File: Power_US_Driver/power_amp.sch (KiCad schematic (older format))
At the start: 9 parts, among them J2 Conn_Coaxial, Q1 Q_NMOS_DGS, Q2 Q_NMOS_DGS, U2 IR2110

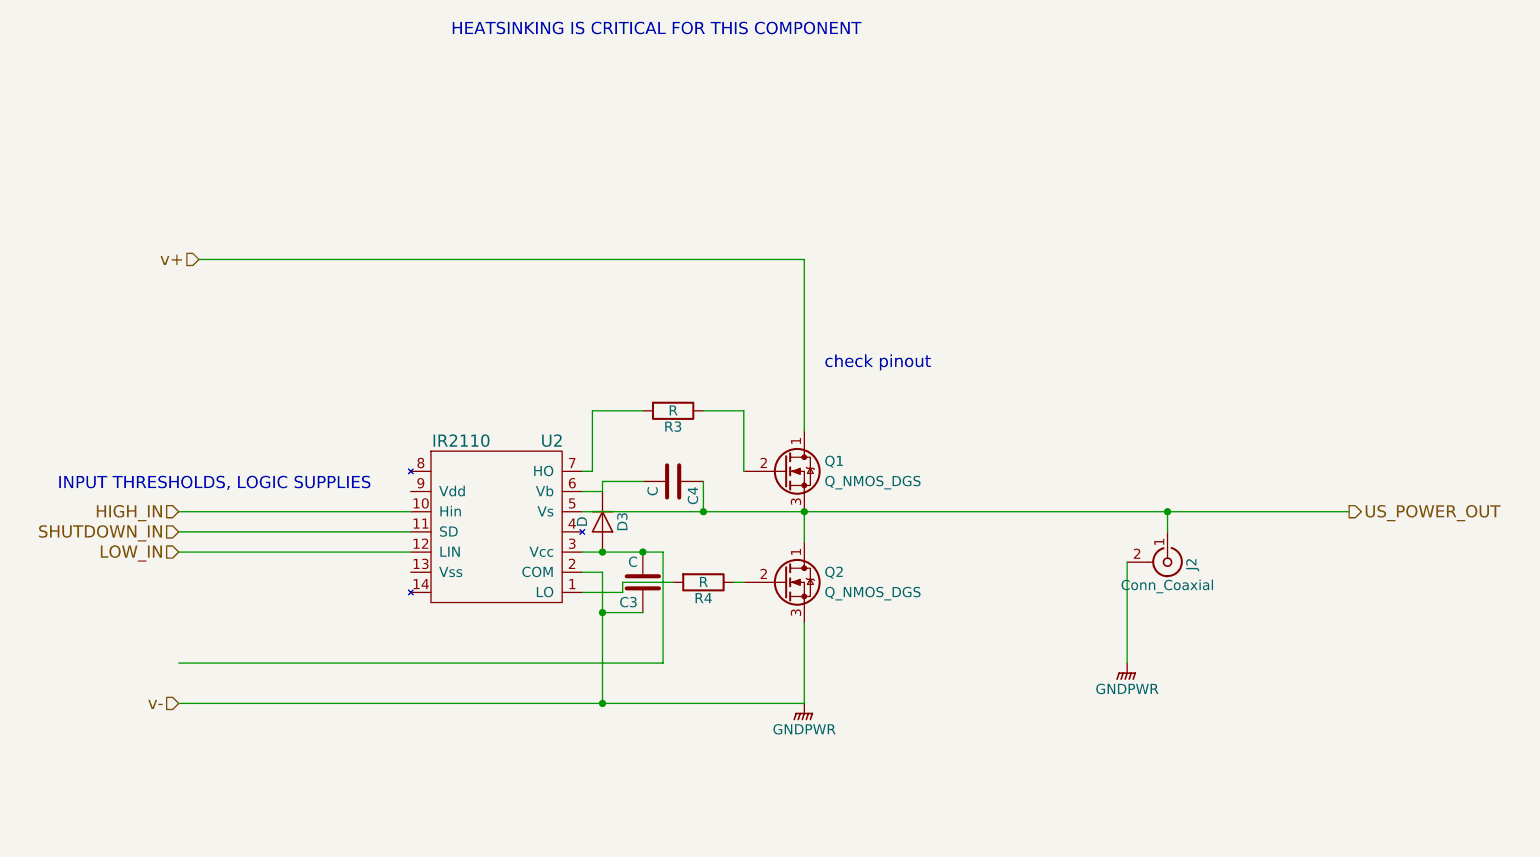
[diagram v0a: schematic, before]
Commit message: CURRENT SENSE REROUT, HIGHSIDE DRIVER GROUNDING
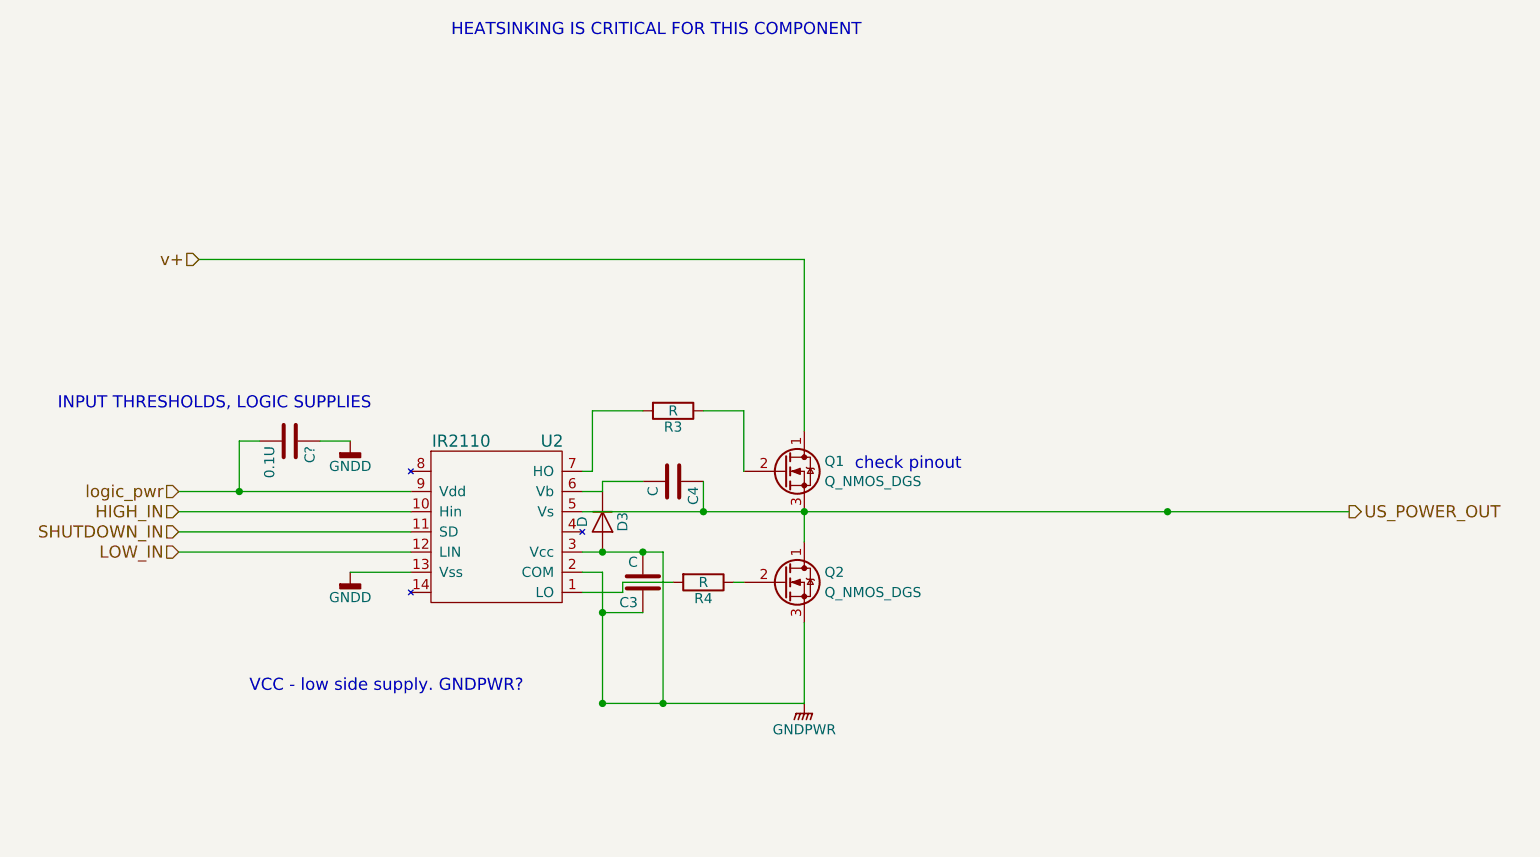
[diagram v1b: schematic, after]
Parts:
- removed J2: Conn_Coaxial, symbol Conn_Coaxial
- added C?: 0.1U, symbol C
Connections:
- net labels added: GNDD, logic_pwr
- net labels removed: v-
- wire segments 30 -> 32
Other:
- note added: "VCC - low side supply. GNDPWR?"
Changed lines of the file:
@@
 LIBS:LIA-cache
 LIBS:power_US
+LIBS:JasMoH_Parts
 LIBS:Power_US_Driver-cache
 EELAYER 25 0
@@
 Text HLabel 3250 2550 0    60   Input ~ 0
 v+
-Text HLabel 3150 4750 0    60   Input ~ 0
-v-
-$Comp
-L Conn_Coaxial J2
-U 1 1 5AADA1B5
-P 8050 4050
-F 0 "J2" H 8060 4170 50  0000 C CNN
-F 1 "Conn_Coaxial" V 8165 4050 50  0000 C CNN
-F 2 "" H 8050 4050 50  0001 C CNN
-F 3 "" H 8050 4050 50  0001 C CNN
-	1    8050 4050
-	0    1    1    0
-$EndComp
 Text Notes 4500 1450 0    60   ~ 0
 HEATSINKING IS CRITICAL FOR THIS COMPONENT
@@
 	1    0    0    -1
 $EndComp
-Text Notes 6350 3100 0    60   ~ 0
+Text Notes 6500 3600 0    60   ~ 0
 check pinout
 $Comp
@@
 $EndComp
 Wire Wire Line
-	7850 4550 7850 4050
-Wire Wire Line
-	8050 3800 8050 3900
-Wire Wire Line
 	5150 3800 8950 3800
 Wire Wire Line
@@
 Wire Wire Line
 	6250 4750 6250 4350
-Wire Wire Line
-	3150 4750 6250 4750
 Connection ~ 8050 3800
 Wire Wire Line
@@
 Connection ~ 5250 4000
 Wire Wire Line
-	5550 4000 5550 4550
-Wire Wire Line
-	5550 4550 3150 4550
+	5550 4000 5550 4750
 Connection ~ 5450 4000
-Text Notes 2550 3700 0    60   ~ 0
+Text Notes 2550 3300 0    60   ~ 0
 INPUT THRESHOLDS, LOGIC SUPPLIES
 $Comp
-L GNDPWR #PWR?
+L GNDPWR #PWR8
 U 1 1 5AB00C48
 P 6250 4750
-F 0 "#PWR?" H 6250 4550 50  0001 C CNN
+F 0 "#PWR8" H 6250 4550 50  0001 C CNN
 F 1 "GNDPWR" H 6250 4620 50  0000 C CNN
 F 2 "" H 6250 4700 50  0001 C CNN
@@
 $EndComp
 $Comp
-L GNDPWR #PWR?
-U 1 1 5AB01180
-P 7850 4550
-F 0 "#PWR?" H 7850 4350 50  0001 C CNN
-F 1 "GNDPWR" H 7850 4420 50  0000 C CNN
-F 2 "" H 7850 4500 50  0001 C CNN
-F 3 "" H 7850 4500 50  0001 C CNN
-	1    7850 4550
-	1    0    0    -1
-$EndComp
+L GNDD #PWR?
+U 1 1 5AB1B5F8
+P 4000 4100
+F 0 "#PWR?" H 4000 3850 50  0001 C CNN
+F 1 "GNDD" H 4000 3975 50  0000 C CNN
+F 2 "" H 4000 4100 50  0001 C CNN
+F 3 "" H 4000 4100 50  0001 C CNN
+	1    4000 4100
+	1    0    0    -1
+$EndComp
+Wire Wire Line
+	4300 4100 4000 4100
+Text HLabel 3150 3700 0    60   Input ~ 0
+logic_pwr
+Wire Wire Line
+	3150 3700 4300 3700
+Text Notes 3500 4700 0    60   ~ 0
+VCC - low side supply. GNDPWR?
+$Comp
+L C C?
+U 1 1 5AB1B9D2
+P 3700 3450
+F 0 "C?" H 3725 3550 50  0000 L CNN
+F 1 "0.1U" H 3725 3350 50  0000 L CNN
+F 2 "" H 3738 3300 50  0001 C CNN
+F 3 "" H 3700 3450 50  0001 C CNN
+	1    3700 3450
+	0    1    1    0
+$EndComp
+$Comp
+L GNDD #PWR?
+U 1 1 5AB1BA1D
+P 4000 3450
+F 0 "#PWR?" H 4000 3200 50  0001 C CNN
+F 1 "GNDD" H 4000 3325 50  0000 C CNN
+F 2 "" H 4000 3450 50  0001 C CNN
+F 3 "" H 4000 3450 50  0001 C CNN
+	1    4000 3450
+	1    0    0    -1
+$EndComp
+Wire Wire Line
+	4000 3450 3850 3450
+Wire Wire Line
+	3550 3450 3450 3450
+Wire Wire Line
+	3450 3450 3450 3700
+Connection ~ 3450 3700
+Connection ~ 5550 4750
+Wire Wire Line
+	5250 4750 6250 4750
 $EndSCHEMATC

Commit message: initial Current sense more vacilating over power drive solution
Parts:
- gave numbers to parts that had none: 1
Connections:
- net GNDPWR: no longer C3.1, C3.2, D3.2 (A), Q2.3 (S), U2.2 (COM), U2.3 (Vcc)
- net at Q2.2 (G): no longer R4.1
- new net V-: C3.1, C3.2, D3.2 (A), Q2.3 (S), U2.2 (COM), U2.3 (Vcc)
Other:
- note added: "C, R values"
- note added: "check that -60 is ok"
- note added: "has to be dragged to V- to turn off..."
- note added: "two of these and an optoisolator?"
- moved on the sheet: R4
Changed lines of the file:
@@
 check pinout
-$Comp
-L Q_NMOS_DGS Q2
-U 1 1 5AAE8077
-P 6150 4150
-F 0 "Q2" H 6350 4200 50  0000 L CNN
-F 1 "Q_NMOS_DGS" H 6350 4100 50  0000 L CNN
-F 2 "" H 6350 4250 50  0001 C CNN
-F 3 "" H 6150 4150 50  0001 C CNN
-	1    6150 4150
-	1    0    0    -1
-$EndComp
 $Comp
 L IR2110 U2
@@
 L R R4
 U 1 1 5AAE9F5C
-P 5750 4150
-F 0 "R4" V 5830 4150 50  0000 C CNN
-F 1 "R" V 5750 4150 50  0000 C CNN
-F 2 "" V 5680 4150 50  0001 C CNN
-F 3 "" H 5750 4150 50  0001 C CNN
-	1    5750 4150
-	0    1    1    0
-$EndComp
-Wire Wire Line
-	5150 3800 8950 3800
+P 5700 4300
+F 0 "R4" V 5780 4300 50  0000 C CNN
+F 1 "R" V 5700 4300 50  0000 C CNN
+F 2 "" V 5630 4300 50  0001 C CNN
+F 3 "" H 5700 4300 50  0001 C CNN
+	1    5700 4300
+	-1   0    0    1
+$EndComp
+Wire Wire Line
+	5150 3800 5750 3800
+Wire Wire Line
+	5750 3800 6250 3800
+Wire Wire Line
+	6250 3800 8050 3800
+Wire Wire Line
+	8050 3800 8950 3800
 Wire Wire Line
 	6250 3800 6250 3950
@@
 Connection ~ 8050 3800
 Wire Wire Line
-	5900 4150 5950 4150
-Wire Wire Line
-	5600 4150 5350 4150
+	5350 4150 5700 4150
 Wire Wire Line
 	5350 4150 5350 4200
@@
 Connection ~ 6250 3800
 Wire Wire Line
-	5250 4100 5250 4750
+	5250 4100 5250 4300
+Wire Wire Line
+	5250 4300 5250 4750
 Connection ~ 5250 4750
 Text HLabel 3150 4000 0    60   Input ~ 0
@@
 $EndComp
 Wire Wire Line
-	5150 4000 5550 4000
+	5150 4000 5250 4000
+Wire Wire Line
+	5250 4000 5450 4000
+Wire Wire Line
+	5450 4000 5550 4000
 $Comp
 L D D3
@@
 INPUT THRESHOLDS, LOGIC SUPPLIES
 $Comp
-L GNDPWR #PWR8
+L GNDPWR #PWR13
 U 1 1 5AB00C48
-P 6250 4750
-F 0 "#PWR8" H 6250 4550 50  0001 C CNN
-F 1 "GNDPWR" H 6250 4620 50  0000 C CNN
-F 2 "" H 6250 4700 50  0001 C CNN
-F 3 "" H 6250 4700 50  0001 C CNN
-	1    6250 4750
-	1    0    0    -1
-$EndComp
-$Comp
-L GNDD #PWR?
+P 6500 5250
+F 0 "#PWR13" H 6500 5050 50  0001 C CNN
+F 1 "GNDPWR" H 6500 5120 50  0000 C CNN
+F 2 "" H 6500 5200 50  0001 C CNN
+F 3 "" H 6500 5200 50  0001 C CNN
+	1    6500 5250
+	1    0    0    -1
+$EndComp
+$Comp
+L GNDD #PWR12
 U 1 1 5AB1B5F8
 P 4000 4100
-F 0 "#PWR?" H 4000 3850 50  0001 C CNN
+F 0 "#PWR12" H 4000 3850 50  0001 C CNN
 F 1 "GNDD" H 4000 3975 50  0000 C CNN
 F 2 "" H 4000 4100 50  0001 C CNN
@@
 logic_pwr
 Wire Wire Line
-	3150 3700 4300 3700
+	3150 3700 3450 3700
+Wire Wire Line
+	3450 3700 4300 3700
 Text Notes 3500 4700 0    60   ~ 0
 VCC - low side supply. GNDPWR?
 $Comp
-L C C?
+L C C8
 U 1 1 5AB1B9D2
 P 3700 3450
-F 0 "C?" H 3725 3550 50  0000 L CNN
+F 0 "C8" H 3725 3550 50  0000 L CNN
 F 1 "0.1U" H 3725 3350 50  0000 L CNN
 F 2 "" H 3738 3300 50  0001 C CNN
@@
 $EndComp
 $Comp
-L GNDD #PWR?
+L GNDD #PWR11
 U 1 1 5AB1BA1D
 P 4000 3450
-F 0 "#PWR?" H 4000 3200 50  0001 C CNN
+F 0 "#PWR11" H 4000 3200 50  0001 C CNN
 F 1 "GNDD" H 4000 3325 50  0000 C CNN
 F 2 "" H 4000 3450 50  0001 C CNN
@@
 Connection ~ 5550 4750
 Wire Wire Line
-	5250 4750 6250 4750
+	3100 4750 5250 4750
+Wire Wire Line
+	5250 4750 5550 4750
+Wire Wire Line
+	5550 4750 6250 4750
+Text HLabel 3100 4750 0    60   Input ~ 0
+V-
+Text Notes 3550 4850 0    60   ~ 0
+check that -60 is ok
+Text Notes 5200 3200 0    60   ~ 0
+C, R values
+$Comp
+L Q_NMOS_DGS Q2
+U 1 1 5AAE8077
+P 6150 4150
+F 0 "Q2" H 6350 4200 50  0000 L CNN
+F 1 "Q_NMOS_DGS" H 6350 4100 50  0000 L CNN
+F 2 "" H 6350 4250 50  0001 C CNN
+F 3 "" H 6150 4150 50  0001 C CNN
+	1    6150 4150
+	1    0    0    -1
+$EndComp
+Connection ~ 5700 4150
+Connection ~ 6000 4750
+Text Notes 6950 4150 0    60   ~ 0
+has to be dragged to V- to turn off...
+Text Notes 3900 5250 0    60   ~ 0
+two of these and an optoisolator?
 $EndSCHEMATC

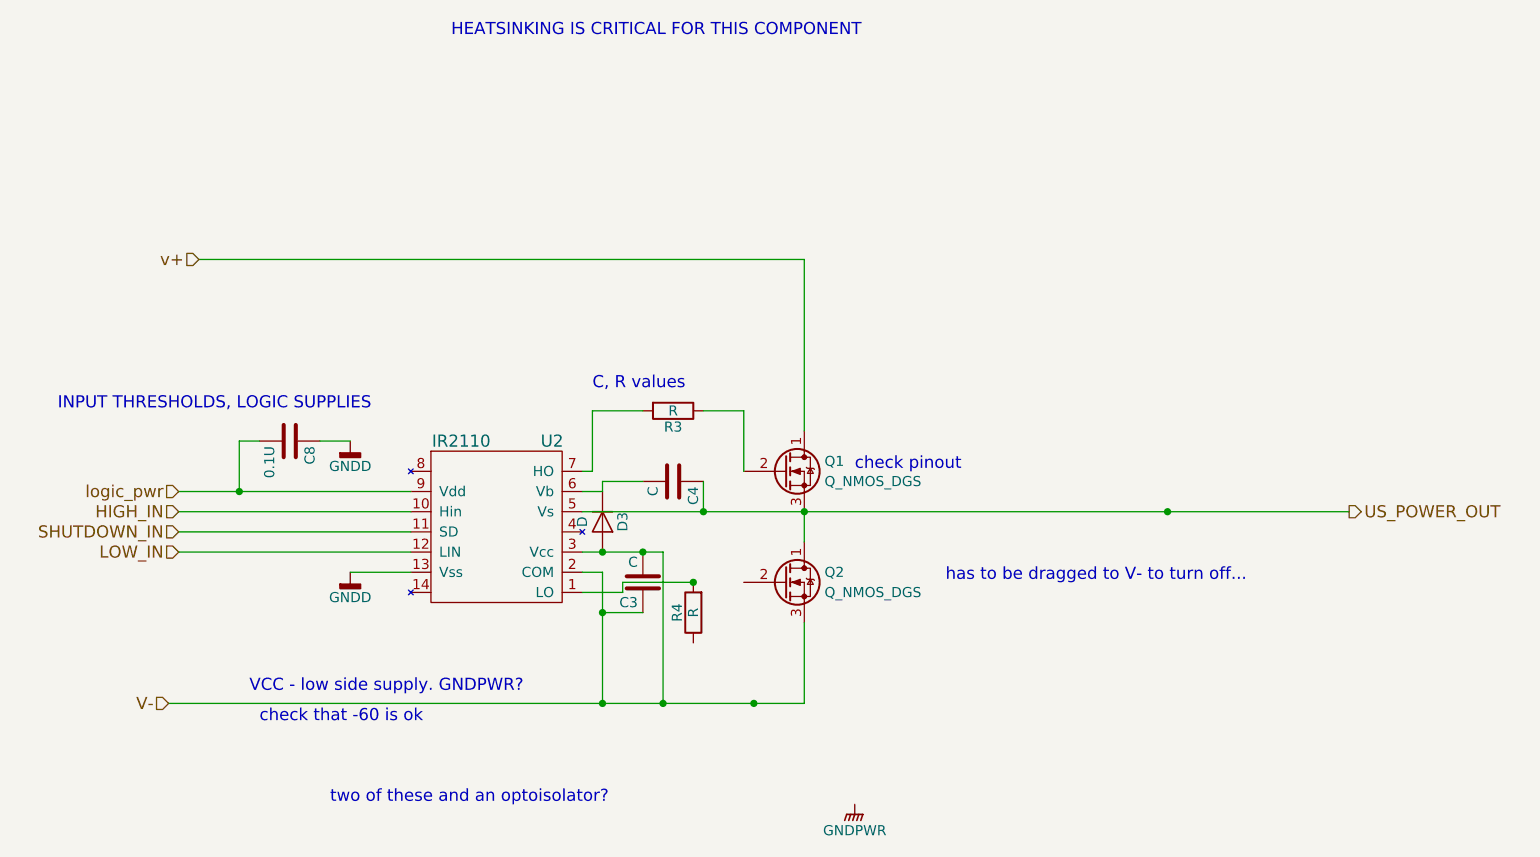
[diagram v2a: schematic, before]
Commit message: Screw it, 0-120V output voltage is fine for a cheapo first pass
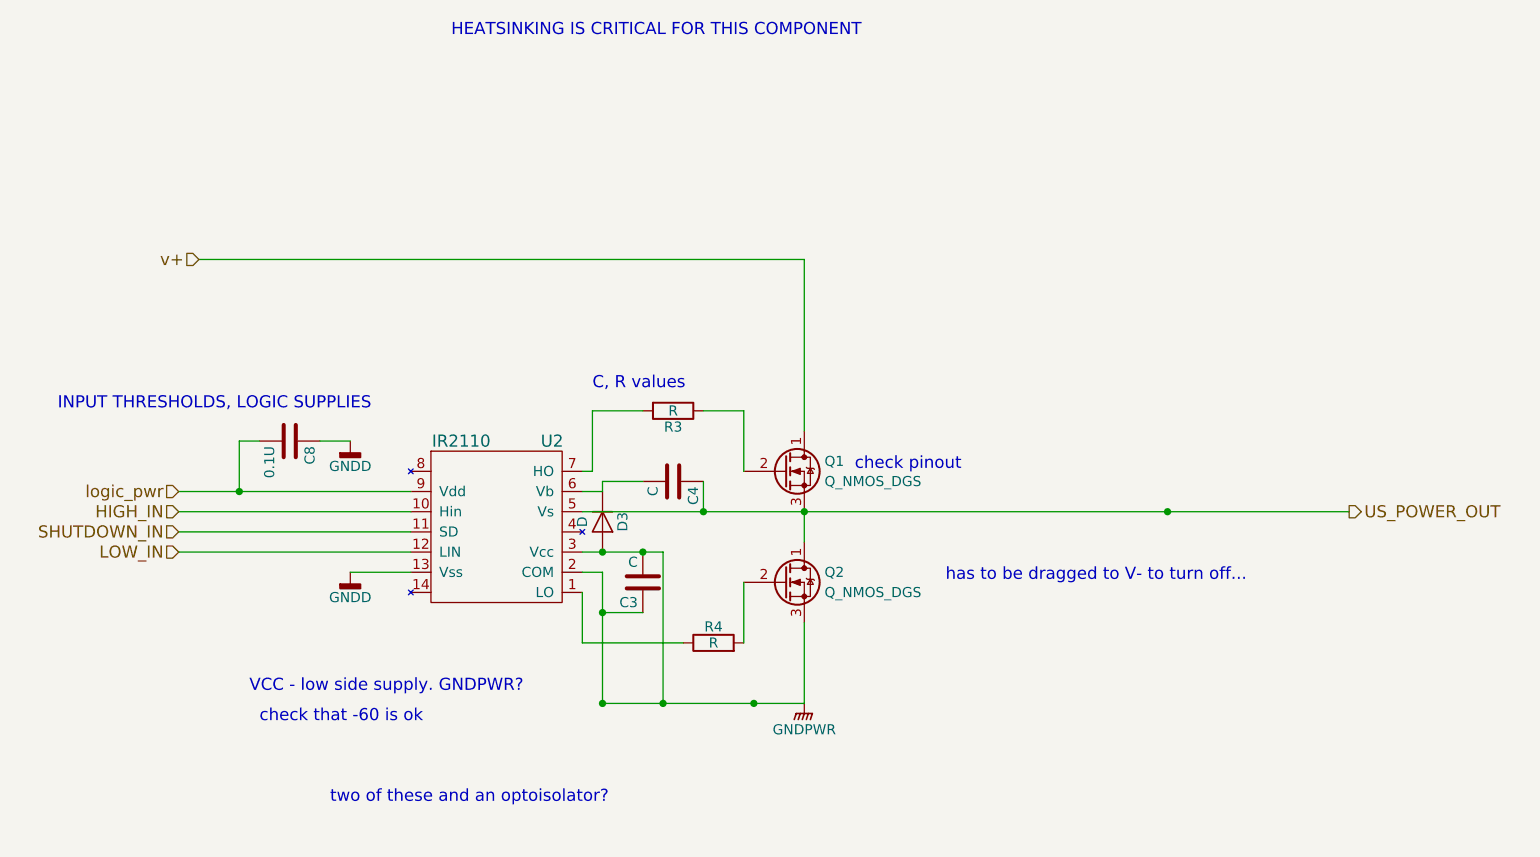
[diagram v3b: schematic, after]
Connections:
- net V- is gone; now on net GNDPWR: C3.1, C3.2, D3.2 (A), Q2.3 (S), U2.2 (COM), U2.3 (Vcc)
- net at Q2.2 (G): now also R4.2
- net at U2.1 (LO): now also R4.1; no longer R4.2
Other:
- moved on the sheet: R4
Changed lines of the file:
@@
 L R R4
 U 1 1 5AAE9F5C
-P 5700 4300
-F 0 "R4" V 5780 4300 50  0000 C CNN
-F 1 "R" V 5700 4300 50  0000 C CNN
-F 2 "" V 5630 4300 50  0001 C CNN
-F 3 "" H 5700 4300 50  0001 C CNN
-	1    5700 4300
-	-1   0    0    1
-$EndComp
-Wire Wire Line
-	5150 3800 5750 3800
-Wire Wire Line
-	5750 3800 6250 3800
-Wire Wire Line
-	6250 3800 8050 3800
-Wire Wire Line
-	8050 3800 8950 3800
+P 5800 4450
+F 0 "R4" V 5880 4450 50  0000 C CNN
+F 1 "R" V 5800 4450 50  0000 C CNN
+F 2 "" V 5730 4450 50  0001 C CNN
+F 3 "" H 5800 4450 50  0001 C CNN
+	1    5800 4450
+	0    -1   -1   0
+$EndComp
+Wire Wire Line
+	5150 3800 8950 3800
 Wire Wire Line
 	6250 3800 6250 3950
@@
 	6250 4750 6250 4350
 Connection ~ 8050 3800
-Wire Wire Line
-	5350 4150 5700 4150
-Wire Wire Line
-	5350 4150 5350 4200
-Wire Wire Line
-	5350 4200 5150 4200
 Connection ~ 6250 3800
 Wire Wire Line
-	5250 4100 5250 4300
-Wire Wire Line
-	5250 4300 5250 4750
+	5250 4100 5250 4750
 Connection ~ 5250 4750
 Text HLabel 3150 4000 0    60   Input ~ 0
@@
 $EndComp
 Wire Wire Line
-	5150 4000 5250 4000
-Wire Wire Line
-	5250 4000 5450 4000
-Wire Wire Line
-	5450 4000 5550 4000
+	5150 4000 5550 4000
 $Comp
 L D D3
@@
 L GNDPWR #PWR13
 U 1 1 5AB00C48
-P 6500 5250
-F 0 "#PWR13" H 6500 5050 50  0001 C CNN
-F 1 "GNDPWR" H 6500 5120 50  0000 C CNN
-F 2 "" H 6500 5200 50  0001 C CNN
-F 3 "" H 6500 5200 50  0001 C CNN
-	1    6500 5250
+P 6250 4750
+F 0 "#PWR13" H 6250 4550 50  0001 C CNN
+F 1 "GNDPWR" H 6250 4620 50  0000 C CNN
+F 2 "" H 6250 4700 50  0001 C CNN
+F 3 "" H 6250 4700 50  0001 C CNN
+	1    6250 4750
 	1    0    0    -1
 $EndComp
@@
 logic_pwr
 Wire Wire Line
-	3150 3700 3450 3700
-Wire Wire Line
-	3450 3700 4300 3700
+	3150 3700 4300 3700
 Text Notes 3500 4700 0    60   ~ 0
 VCC - low side supply. GNDPWR?
@@
 Connection ~ 3450 3700
 Connection ~ 5550 4750
-Wire Wire Line
-	3100 4750 5250 4750
-Wire Wire Line
-	5250 4750 5550 4750
-Wire Wire Line
-	5550 4750 6250 4750
-Text HLabel 3100 4750 0    60   Input ~ 0
-V-
 Text Notes 3550 4850 0    60   ~ 0
 check that -60 is ok
@@
 	1    0    0    -1
 $EndComp
-Connection ~ 5700 4150
 Connection ~ 6000 4750
 Text Notes 6950 4150 0    60   ~ 0
@@
 Text Notes 3900 5250 0    60   ~ 0
 two of these and an optoisolator?
+Wire Wire Line
+	5150 4200 5150 4450
+Wire Wire Line
+	5150 4450 5650 4450
+Wire Wire Line
+	5950 4450 5950 4150
+Wire Wire Line
+	5250 4750 6250 4750
 $EndSCHEMATC
